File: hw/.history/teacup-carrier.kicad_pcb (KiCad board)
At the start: 4 copper layers, 257 x 117.5 mm, 137 parts, among them J1 AH58893-T9B10-3F, J2 TYPE-C-31-M-12, J20 HDR_J20, J21 HDR_J21, J22 HDR_J22, J23 HDR_J23, J24 HDR_J24, J25 HDR_J25, J26 HDR_J26, J27 HDR_J27, J28 HDR_J28, J29 HDR_J29, J3 TE_292303-7, J30 HDR_J30, J31 HDR_J31, J32 HDR_J32, J33 HDR_J33, J34 HDR_J34, J35 HDR_J35, J36 HDR_J36, J37 HDR_J37, J38 AMP_MIC_TAP, J4 Hirose_DM3D-SF, J5 Wuerth_694106301002, J6 AudioJack4_Ground, J7 SFW15R-2STE1LF, J8 SFW15R-2STE1LF, J9 TYPE-C-31-M-12, Q1 AO3401A, Q2 AO3401A, SW1 SSSS711403, SW2 SSSS711403, U1 AP62600SJ-7, U10 TS5A3166, U11 DIP-8 Socket, U12 TPS2053BDR, U13 W25Q32JVSS, U14 TPS22990DMLR, U15 TCA9555PWR, U2 AP62300WU-7, U3 MCP4661-104E_ST, U4 TPS22990DMLR, U5 AZ1117CH-3.3TRG1, U6 AZ1117CH-1.8TRG1, U7 AP62300WU-7, U8 ESP32-S3-WROOM-1-N16R2, U9 TS5A3166

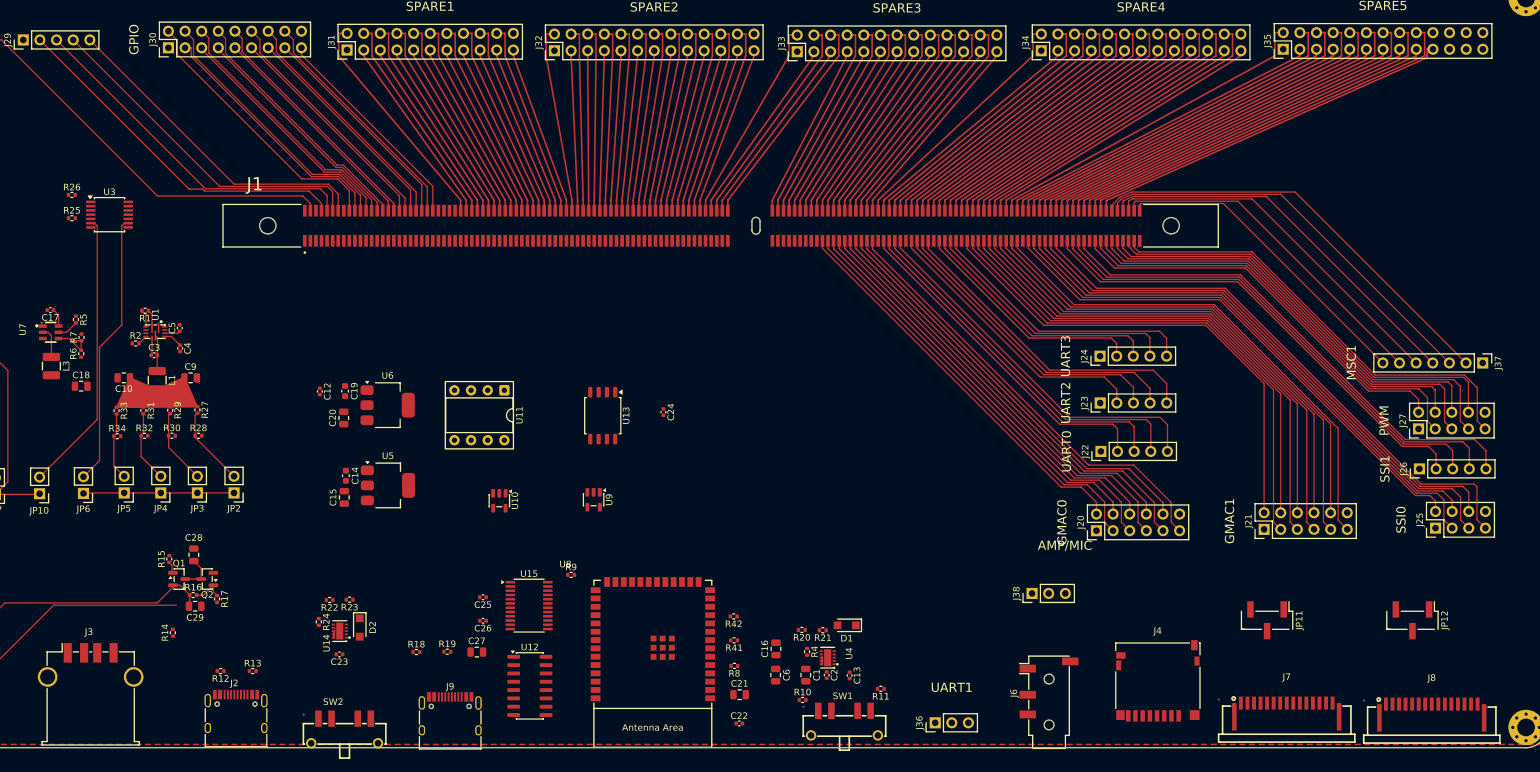
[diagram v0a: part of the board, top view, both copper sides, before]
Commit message: Reorder J1 MSC0/USB-host/ESP-hosted/MIPI1 pins for board-order and grouping
- MSC0 (J1 pins 50/52-56): reordered to match J4's microSD pins in
  actual left-to-right board position (D1/D0/CLK/CMD/D3_CD/D2), not
  J4's raw pin numbers -- J4 sits mirrored relative to J1 on the real
  board, so matching by pin number alone produced a fully-crossed
  assignment.
- USBA_HOST_DP/DM shifted down to pins 40/41, freeing pin 42 for
  HOSTED_RESET so all ESP-Hosted signals (reset + SPI + handshake) are
  one contiguous block (42-48) instead of HOSTED_RESET sitting alone at
  unit 2 pin 86. Pin 86 is now GND.
- MIPI1 pins 73-75 rotated (GPIO/SDA/SCL -> SDA/SCL/GPIO) to match
  MIPI0's arrangement.

PCB updated to match: pad nets reassigned for all of the above, and the
already-routed MSC0/MIPI1 SDA+SCL traces had their J1-side endpoints
moved to the new pad positions rather than left stale. GND zone
refilled and DRC-clean for all touched nets.
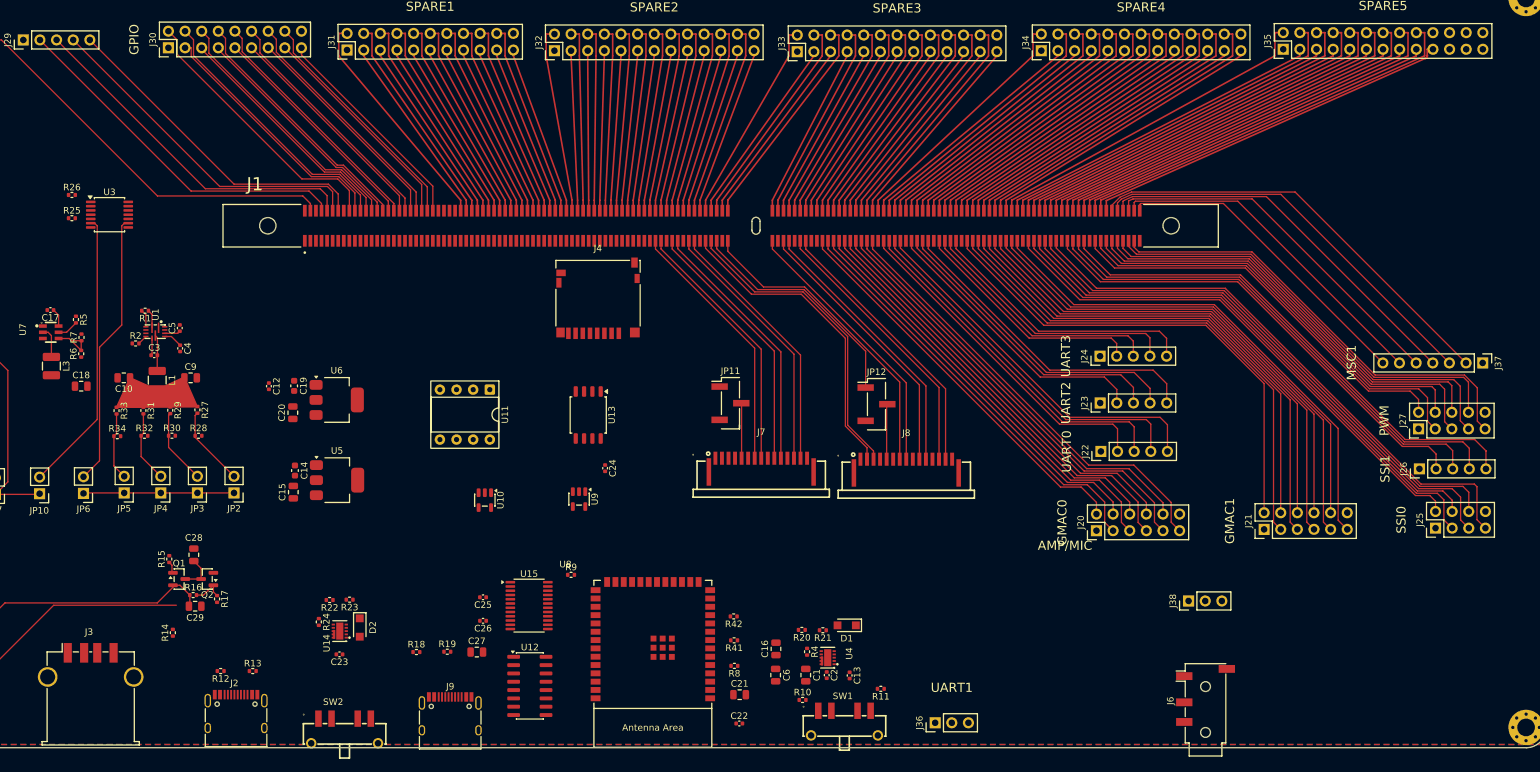
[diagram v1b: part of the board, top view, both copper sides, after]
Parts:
- moved J4 103.6 mm to (130.2, 73.2)
- moved J7 88.5 mm to (155.2, 98.7)
- moved J8 88.5 mm to (177.3, 98.8)
- moved JP11 88.4 mm to (150.4, 89.2), turned to 0 degrees
- moved JP12 88.3 mm to (172.8, 89.4), turned to 0 degrees
- moved J38 23.9 mm to (220.4, 119.5)
- moved J6 23.9 mm to (223.0, 134.8)
- moved C24 12.3 mm to (131.3, 99.2)
- moved C19 7.82 mm to (83.8, 86.6)
- moved C12 7.82 mm to (80.0, 86.7)
- moved C14 7.82 mm to (83.9, 99.5)
- moved C15 7.82 mm to (83.7, 102.8)
- moved C20 7.82 mm to (83.6, 90.7)
- moved U5 7.82 mm to (90.4, 101.0)
- moved U6 7.82 mm to (90.3, 88.8)
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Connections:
- J1 pad 40: GND -> USBA_HOST_DP
- J1 pad 41: USBA_HOST_DP -> USBA_HOST_DM
- J1 pad 42: USBA_HOST_DM -> HOSTED_RESET
- J1 pad 50: MSC0_CLK -> MSC0_D1
- J1 pad 52: MSC0_CMD -> MSC0_D0
- J1 pad 53: MSC0_D0 -> MSC0_CLK
- J1 pad 54: MSC0_D1 -> MSC0_CMD
- J1 pad 55: MSC0_D2 -> MSC0_D3_CD
- J1 pad 56: MSC0_D3_CD -> MSC0_D2
- J1 pad 73: MIPI1_GPIO -> MIPI1_SCCB_SDA
- J1 pad 74: MIPI1_SCCB_SDA -> MIPI1_SCCB_SCL
- J1 pad 75: MIPI1_SCCB_SCL -> MIPI1_GPIO
- J1 pad 86: HOSTED_RESET -> GND
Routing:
- net MIPI1_SCCB_SDA: track 0.00 -> 48.0 mm
- net MIPI1_SCCB_SCL: track 0.00 -> 47.9 mm
- net MIPI1_CLKP: track 0.00 -> 47.9 mm
- net MIPI1_D0N: track 0.00 -> 42.2 mm
- net MIPI1_D0P: track 0.00 -> 42.1 mm
- net MIPI1_D1N: track 0.00 -> 42.0 mm
- net MIPI1_D1P: track 0.00 -> 41.9 mm
- net MIPI1_CLKN: track 0.00 -> 41.8 mm
- net MIPI0_D0N: track 0.00 -> 39.9 mm
- net MIPI0_D0P: track 0.00 -> 39.8 mm
- net MIPI0_D1N: track 0.00 -> 39.7 mm
- net MIPI0_D1P: track 0.00 -> 39.7 mm
- net MIPI0_CLKN: track 0.00 -> 39.5 mm
- net MIPI0_CLKP: track 0.00 -> 39.5 mm
- net MIPI1_GPIO: track 0.00 -> 36.0 mm
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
